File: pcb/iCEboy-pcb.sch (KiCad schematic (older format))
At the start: 64 parts, among them J1 DMG_CARD, J2 PROG_PORT, Q1 2N7002K, U1 TC74LCXR163245FT, U2 TC74LCXR163245FT, U3 ICE40UP5K-SG48ITR, U4 TPS79901DDCR, U5 TPS79901DDCR, U6 W25Q80DVSSIG, X1 SIT2001B 20MHz

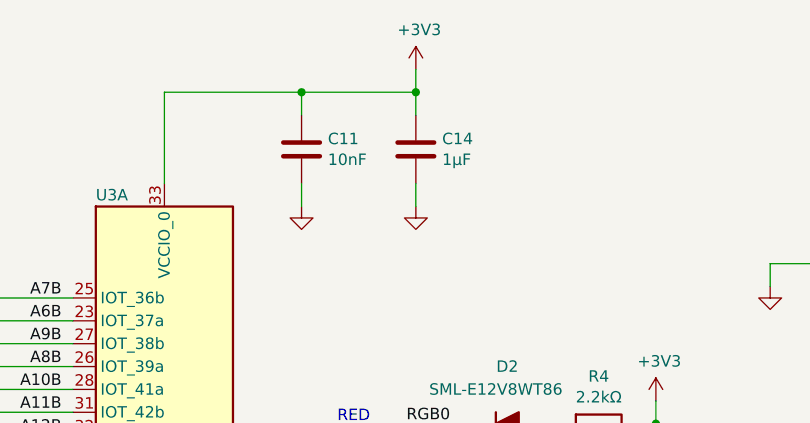
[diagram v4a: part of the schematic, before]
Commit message: swap C11 C14 value
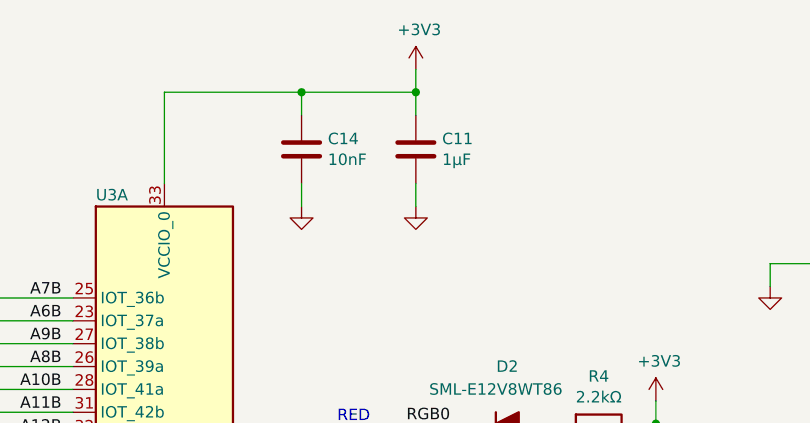
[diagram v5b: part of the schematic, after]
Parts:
- C11: value 10nF -> 1μF
- C14: value 1μF -> 10nF
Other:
- moved on the sheet: C11, C14
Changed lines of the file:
@@
 L Device:C C14
 U 1 1 6060DD49
-P 9000 1550
-F 0 "C14" H 9115 1596 50  0000 L CNN
-F 1 "1μF" H 9115 1505 50  0000 L CNN
-F 2 "Capacitor_SMD:C_0603_1608Metric" H 9038 1400 50  0001 C CNN
-F 3 "~" H 9000 1550 50  0001 C CNN
-	1    9000 1550
+P 8500 1550
+F 0 "C14" H 8615 1596 50  0000 L CNN
+F 1 "10nF" H 8615 1505 50  0000 L CNN
+F 2 "Capacitor_SMD:C_0603_1608Metric" H 8538 1400 50  0001 C CNN
+F 3 "~" H 8500 1550 50  0001 C CNN
+	1    8500 1550
 	1    0    0    -1
 $EndComp
@@
 L Device:C C11
 U 1 1 6060DD6B
-P 8500 1550
-F 0 "C11" H 8615 1596 50  0000 L CNN
-F 1 "10nF" H 8615 1505 50  0000 L CNN
-F 2 "Capacitor_SMD:C_0603_1608Metric" H 8538 1400 50  0001 C CNN
-F 3 "~" H 8500 1550 50  0001 C CNN
-	1    8500 1550
+P 9000 1550
+F 0 "C11" H 9115 1596 50  0000 L CNN
+F 1 "1μF" H 9115 1505 50  0000 L CNN
+F 2 "Capacitor_SMD:C_0603_1608Metric" H 9038 1400 50  0001 C CNN
+F 3 "~" H 9000 1550 50  0001 C CNN
+	1    9000 1550
 	1    0    0    -1
 $EndComp
@@
 Wire Wire Line
 	14200 7800 14650 7800
-Wire Bus Line
-	2100 7550 2100 10700
-Wire Bus Line
-	11300 8550 11300 10700
-Wire Bus Line
-	9450 7650 9450 9450
-Wire Bus Line
-	12500 2400 12500 3350
-Wire Bus Line
-	8850 2850 8850 4250
-Wire Bus Line
-	7150 3700 7150 4250
-Wire Bus Line
-	10950 2650 10950 7650
-Wire Bus Line
-	7000 6850 7000 7450
-Wire Bus Line
-	10750 2250 10750 3350
-Wire Bus Line
-	6900 9500 6900 10200
-Wire Bus Line
-	6900 5550 6900 6750
-Wire Bus Line
-	2100 4350 2100 5950
-Wire Bus Line
-	2100 6050 2100 7350
-Wire Bus Line
-	3700 3050 3700 5950
-Wire Bus Line
-	5800 7550 5800 9450
-Wire Bus Line
-	5800 3050 5800 4850
-Wire Bus Line
-	6900 2300 6900 4850
-Wire Bus Line
-	3700 7350 3700 9250
 Text Notes 8800 2750 2    50   ~ 0
 RED
@@
 Text Notes 9250 6850 0    50   ~ 0
 YELLOW
+Wire Bus Line
+	2100 7550 2100 10700
+Wire Bus Line
+	11300 8550 11300 10700
+Wire Bus Line
+	9450 7650 9450 9450
+Wire Bus Line
+	12500 2400 12500 3350
+Wire Bus Line
+	8850 2850 8850 4250
+Wire Bus Line
+	7150 3700 7150 4250
+Wire Bus Line
+	10950 2650 10950 7650
+Wire Bus Line
+	7000 6850 7000 7450
+Wire Bus Line
+	10750 2250 10750 3350
+Wire Bus Line
+	6900 9500 6900 10200
+Wire Bus Line
+	6900 5550 6900 6750
+Wire Bus Line
+	2100 4350 2100 5950
+Wire Bus Line
+	2100 6050 2100 7350
+Wire Bus Line
+	3700 3050 3700 5950
+Wire Bus Line
+	5800 7550 5800 9450
+Wire Bus Line
+	5800 3050 5800 4850
+Wire Bus Line
+	6900 2300 6900 4850
+Wire Bus Line
+	3700 7350 3700 9250
 $EndSCHEMATC
